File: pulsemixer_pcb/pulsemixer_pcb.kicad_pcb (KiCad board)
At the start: 2 copper layers, 177.9 x 112 mm, 116 parts, among them Q201 Q_NPN_BEC, Q301 Q_NPN_BEC, Q401 Q_NPN_BEC, Q501 Q_NPN_BEC, SW101 SW_PUSH_SPST, SW102 SW_PUSH_SPST, SW103 SW_PUSH_SPST, SW201 Vol_Encoder, SW202 SW_PUSH_SPST, SW301 Vol_Encoder, SW302 SW_PUSH_SPST, SW401 Vol_Encoder, SW402 SW_PUSH_SPST, SW501 Vol_Encoder, SW502 SW_PUSH_SPST, U101 SN74LHC08DR, U102 SN74HC21DR, U103 74LVC3G17, U201 MCP23017_SP, U202 74LVC2G17, U301 MCP23017_SP, U302 74LVC2G17, U401 MCP23017_SP, U402 74LVC2G17, U501 MCP23017_SP, U502 74LVC2G17

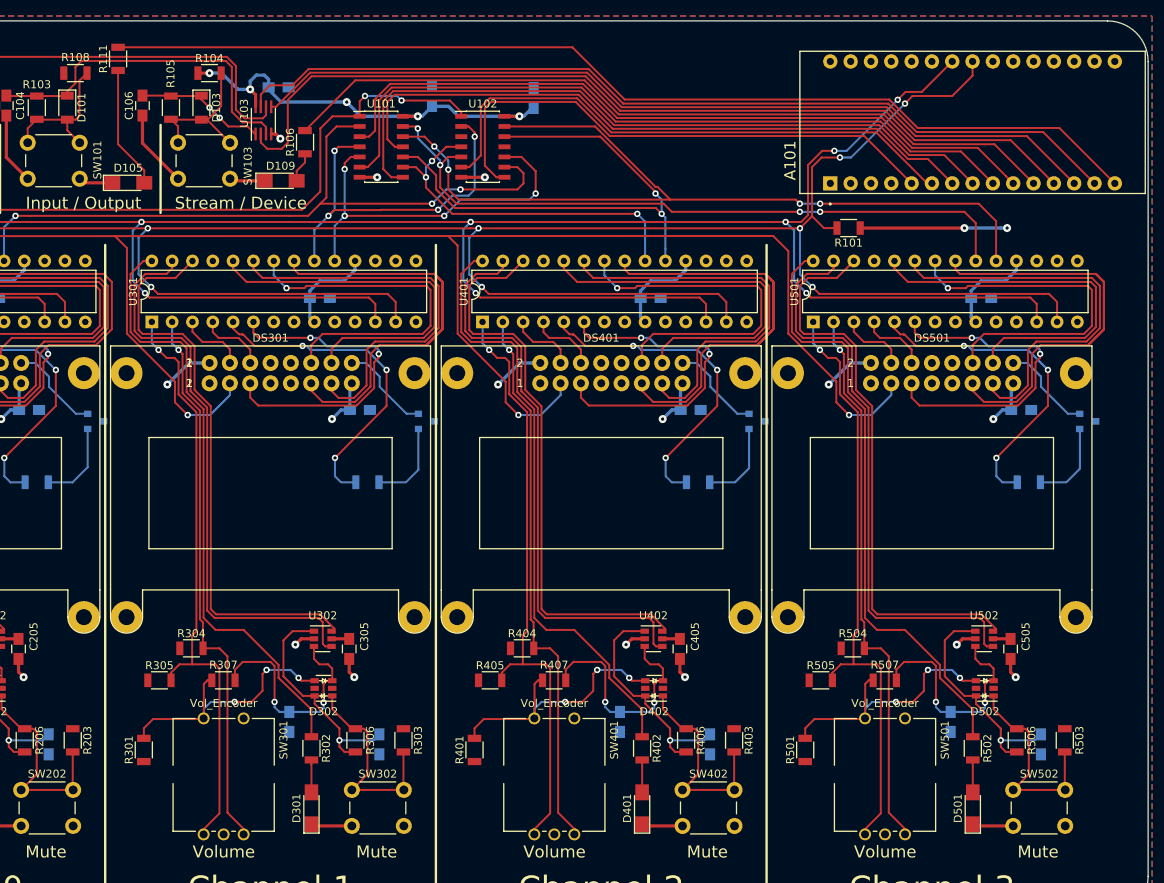
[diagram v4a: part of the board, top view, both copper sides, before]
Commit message: Added another AND gate to include master section buttons in the buttn interrupt logic.
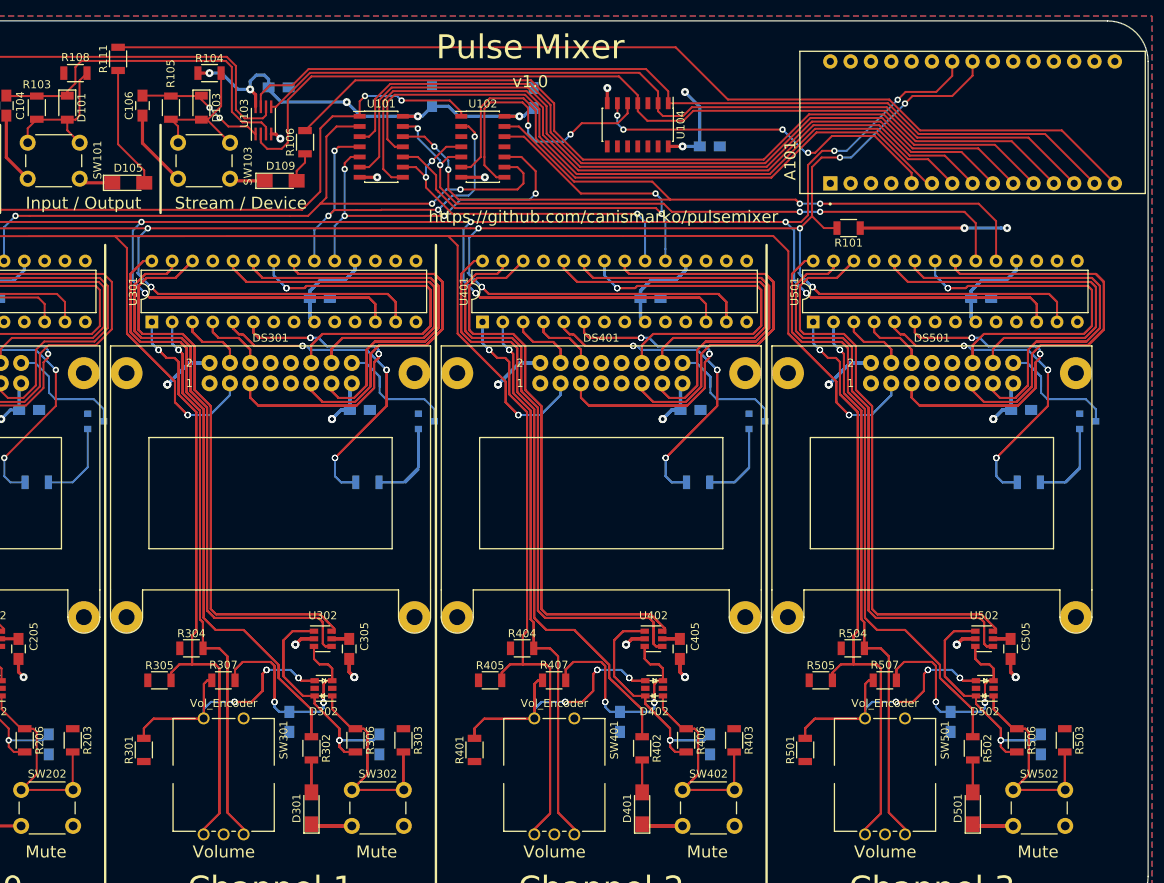
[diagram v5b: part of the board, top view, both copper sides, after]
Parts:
- added C108: 0.1µ, Capacitors_SMD:C_0805_HandSoldering, B.Cu at (183.4, 48.5)
- added U104: SN74HC21DR, Housings_SOIC:SOIC-14_3.9x8.7mm_Pitch1.27mm, F.Cu at (174.4, 45.8)
- D105, D109: value LED -> LED_GREEN
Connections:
- net /STRM_DEV renamed /STRM_DEV_BTN
- net Net-(A101-Pad15) renamed /IO_LED
- Q201 pad 2: /Channel0/LCD_LED- -> GND
- Q201 pad 3: GND -> /Channel0/LCD_LED-
- Q301 pad 2: /Channel1/LCD_LED- -> GND
- Q301 pad 3: GND -> /Channel1/LCD_LED-
- Q401 pad 2: /Channel2/LCD_LED- -> GND
- Q401 pad 3: GND -> /Channel2/LCD_LED-
- Q501 pad 2: /Channel3/LCD_LED- -> GND
- Q501 pad 3: GND -> /Channel3/LCD_LED-
- U102 pad 8: /INTBTN -> /INT_CH_BTN
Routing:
- net /SDA: track 330.4 -> 439.5 mm, vias 10 -> 13
- net /SCK: track 323.0 -> 425.4 mm, vias 10 -> 13
- net +5V: track 180.0 -> 271.7 mm, vias 15 -> 23
- net /Channel2/MUTE_LED: track 75.6 -> 151.2 mm
- net /Channel1/MUTE_LED: track 75.6 -> 151.2 mm
- net /Channel3/MUTE_LED: track 75.6 -> 151.2 mm
- net /Channel3/VOL_A: track 75.1 -> 150.3 mm, vias 1 -> 2
- net /Channel1/VOL_A: track 75.1 -> 150.3 mm, vias 1 -> 2
- net /Channel2/VOL_A: track 75.1 -> 150.3 mm, vias 1 -> 2
- net /Channel2/VOL_SW: track 72.9 -> 145.9 mm
- net /Channel1/VOL_SW: track 72.9 -> 145.9 mm
- net /Channel3/VOL_SW: track 72.9 -> 145.9 mm
- net /Channel2/MUTE_SW: track 72.1 -> 144.1 mm
- net /Channel1/MUTE_SW: track 72.1 -> 144.1 mm
- net /Channel3/MUTE_SW: track 72.1 -> 144.1 mm
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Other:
- board text added: "Pulse Mixer"
- board text added: "https://github.com/canismarko/pulsemixer"
- board text added: "v1.0"

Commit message: Finalized changes to board and sent for fabrication.
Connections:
- U201 pad 15: +5V -> GND
- U301 pad 15: GND -> +5V
- U301 pad 16: +5V -> GND
- U401 pad 15: +5V -> GND
- U501 pad 15: GND -> +5V
- U501 pad 16: GND -> +5V
